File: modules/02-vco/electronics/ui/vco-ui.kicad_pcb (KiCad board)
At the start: 2 copper layers, 58 x 110 mm, 40 parts, among them J1 Conn_01x04, J2 Conn_02x05_Odd_Even, J3 Conn_02x03_Odd_Even, J4 Conn_01x02, J5 Conn_02x02_Counter_Clockwise, J6 Conn_01x07, U1 0203

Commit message: VCO JLCPCB export done for v1.0
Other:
- board text added: "SHMØERGH MODULEUR"
- board text added: "SM-02 VCO UI V1.0 2025 DEC"
- board text removed: "HM-02 VCO UI V0.2 2025 OCT"
- board text removed: "SHMØERGH HOG MODULEUR"

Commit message: KiCAD version updates - PSU + VCO
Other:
- board text added: "SM-02 VCO UI V1.0"
- board text removed: "SM-02 VCO UI V1.0 2025 DEC"
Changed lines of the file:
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@@
 		)
 	)
-	(gr_text "SM-02 VCO UI \nV1.0 2025 DEC"
+	(gr_text "SM-02 VCO UI \nV1.0"
 		(at 153.394 68.5 0)
 		(layer "F.SilkS")
@@
 			(justify left bottom)
 		)
-		(render_cache "SM-02 VCO UI \nV1.0 2025 DEC" 0
+		(render_cache "SM-02 VCO UI \nV1.0" 0
 			(polygon
 				(pts
@@
 				)
 			)
-			(polygon
-				(pts
-					(xy 158.657958 68.011823) (xy 158.657958 68.3045) (xy 159.389789 68.3045) (xy 159.389789 68.158161)
-					(xy 158.804296 68.158161) (xy 158.804296 68.011823)
-				)
-			)
-			(polygon
-				(pts
-					(xy 159.243381 67.279992) (xy 159.243381 67.133584) (xy 158.804296 67.133584) (xy 158.804296 67.279992)
-				)
-			)
-			(polygon
-				(pts
-					(xy 159.243381 67.279992) (xy 159.243381 67.572739) (xy 159.389789 67.572739) (xy 159.389789 67.279992)
-				)
-			)
-			(polygon
-				(pts
-					(xy 158.804296 67.865415) (xy 158.804296 68.011823) (xy 158.950704 68.011823) (xy 158.950704 67.865415)
-				)
-			)
-			(polygon
-				(pts
-					(xy 158.657958 67.279992) (xy 158.657958 67.42633) (xy 158.804296 67.42633) (xy 158.804296 67.279992)
-				)
-			)
-			(polygon
-				(pts
-					(xy 159.097043 67.572739) (xy 159.097043 67.719077) (xy 159.243381 67.719077) (xy 159.243381 67.572739)
-				)
-			)
-			(polygon
-				(pts
-					(xy 158.950704 67.719077) (xy 158.950704 67.865415) (xy 159.097043 67.865415) (xy 159.097043 67.719077)
-				)
-			)
-			(polygon
-				(pts
-					(xy 159.681482 67.279992) (xy 159.681482 68.158161) (xy 159.82782 68.158161) (xy 159.82782 67.865415)
-					(xy 159.974228 67.865415) (xy 159.974228 67.719077) (xy 159.82782 67.719077) (xy 159.82782 67.279992)
-				)
-			)
-			(polygon
-				(pts
-					(xy 159.82782 68.158161) (xy 159.82782 68.3045) (xy 160.266905 68.3045) (xy 160.266905 68.158161)
-				)
-			)
-			(polygon
-				(pts
-					(xy 159.82782 67.133584) (xy 159.82782 67.279992) (xy 160.266905 67.279992) (xy 160.266905 67.133584)
-				)
-			)
-			(polygon
-				(pts
-					(xy 160.266905 67.279992) (xy 160.266905 67.42633) (xy 160.120567 67.42633) (xy 160.120567 67.572739)
-					(xy 160.266905 67.572739) (xy 160.266905 68.158161) (xy 160.413313 68.158161) (xy 160.413313 67.279992)
-				)
-			)
-			(polygon
-				(pts
-					(xy 159.974228 67.572739) (xy 159.974228 67.719077) (xy 160.120567 67.719077) (xy 160.120567 67.572739)
-				)
-			)
-			(polygon
-				(pts
-					(xy 160.705006 68.011823) (xy 160.705006 68.3045) (xy 161.436837 68.3045) (xy 161.436837 68.158161)
-					(xy 160.851344 68.158161) (xy 160.851344 68.011823)
-				)
-			)
-			(polygon
-				(pts
-					(xy 161.290429 67.279992) (xy 161.290429 67.133584) (xy 160.851344 67.133584) (xy 160.851344 67.279992)
-				)
-			)
-			(polygon
-				(pts
-					(xy 161.290429 67.279992) (xy 161.290429 67.572739) (xy 161.436837 67.572739) (xy 161.436837 67.279992)
-				)
-			)
-			(polygon
-				(pts
-					(xy 160.851344 67.865415) (xy 160.851344 68.011823) (xy 160.997753 68.011823) (xy 160.997753 67.865415)
-				)
-			)
-			(polygon
-				(pts
-					(xy 160.705006 67.279992) (xy 160.705006 67.42633) (xy 160.851344 67.42633) (xy 160.851344 67.279992)
-				)
-			)
-			(polygon
-				(pts
-					(xy 161.144091 67.572739) (xy 161.144091 67.719077) (xy 161.290429 67.719077) (xy 161.290429 67.572739)
-				)
-			)
-			(polygon
-				(pts
-					(xy 160.997753 67.719077) (xy 160.997753 67.865415) (xy 161.144091 67.865415) (xy 161.144091 67.719077)
-				)
-			)
-			(polygon
-				(pts
-					(xy 161.72853 67.133584) (xy 161.72853 67.719077) (xy 162.313953 67.719077) (xy 162.313953 67.572739)
-					(xy 161.874868 67.572739) (xy 161.874868 67.279992) (xy 162.460361 67.279992) (xy 162.460361 67.133584)
-				)
-			)
-			(polygon
-				(pts
-					(xy 162.313953 67.719077) (xy 162.313953 68.158161) (xy 162.460361 68.158161) (xy 162.460361 67.719077)
-				)
-			)
-			(polygon
-				(pts
-					(xy 162.313953 68.158161) (xy 161.874868 68.158161) (xy 161.874868 68.3045) (xy 162.313953 68.3045)
-				)
-			)
-			(polygon
-				(pts
-					(xy 161.874868 68.158161) (xy 161.874868 68.011823) (xy 161.72853 68.011823) (xy 161.72853 68.158161)
-				)
-			)
-			(polygon
-				(pts
-					(xy 163.775578 67.133584) (xy 163.775578 68.3045) (xy 164.361001 68.3045) (xy 164.361001 68.158161)
-					(xy 163.921916 68.158161) (xy 163.921916 67.279992) (xy 164.361001 67.279992) (xy 164.361001 67.133584)
-				)
-			)
-			(polygon
-				(pts
-					(xy 164.361001 67.279992) (xy 164.361001 68.158161) (xy 164.507409 68.158161) (xy 164.507409 67.279992)
-				)
-			)
-			(polygon
-				(pts
-					(xy 164.799102 67.133584) (xy 164.799102 68.3045) (xy 165.530933 68.3045) (xy 165.530933 68.158161)
-					(xy 164.945441 68.158161) (xy 164.945441 67.719077) (xy 165.384525 67.719077) (xy 165.384525 67.572739)
-					(xy 164.945441 67.572739) (xy 164.945441 67.279992) (xy 165.530933 67.279992) (xy 165.530933 67.133584)
-				)
-			)
-			(polygon
-				(pts
-					(xy 165.822627 67.279992) (xy 165.822627 68.158161) (xy 165.968965 68.158161) (xy 165.968965 67.279992)
-				)
-			)
-			(polygon
-				(pts
-					(xy 165.968965 68.158161) (xy 165.968965 68.3045) (xy 166.408049 68.3045) (xy 166.408049 68.158161)
-				)
-			)
-			(polygon
-				(pts
-					(xy 166.408049 68.011823) (xy 166.408049 68.158161) (xy 166.554457 68.158161) (xy 166.554457 68.011823)
-				)
-			)
-			(polygon
-				(pts
-					(xy 165.968965 67.133584) (xy 165.968965 67.279992) (xy 166.408049 67.279992) (xy 166.408049 67.133584)
-				)
-			)
-			(polygon
-				(pts
-					(xy 166.408049 67.279992) (xy 166.408049 67.42633) (xy 166.554457 67.42633) (xy 166.554457 67.279992)
-				)
-			)

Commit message: Changed board versioning to 'rev' on VCO and Mixer
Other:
- board text added: "VCO UI REV 1"
- board text removed: "SM-02 VCO UI V1.0"

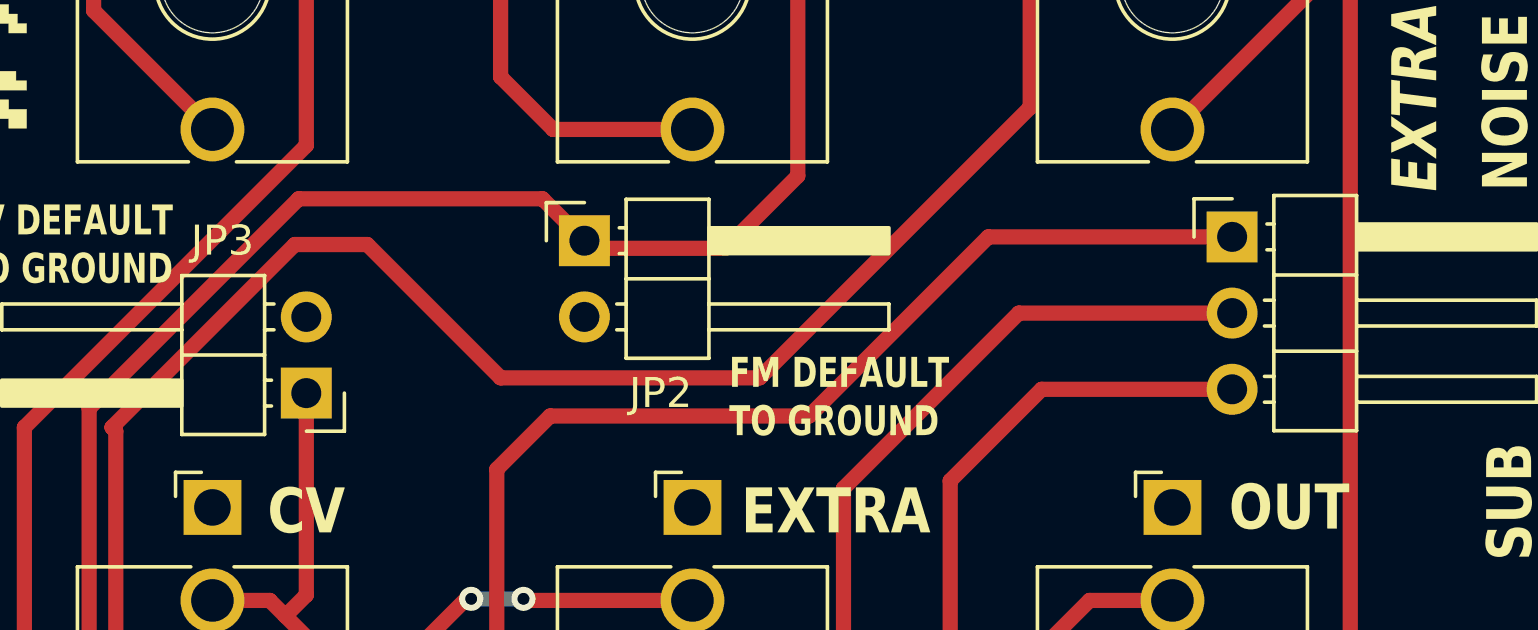
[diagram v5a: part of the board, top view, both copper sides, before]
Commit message: Fixed VCO schemo and PCB after fckckin KiCAD update
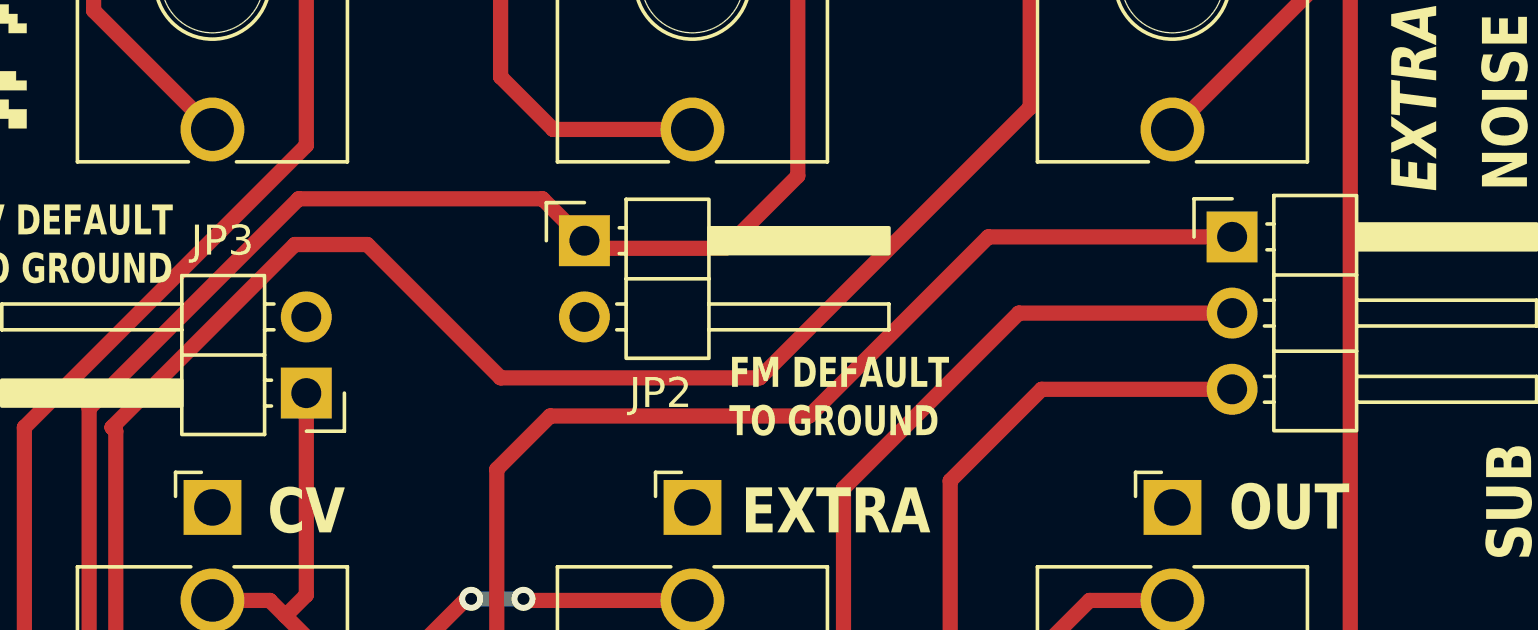
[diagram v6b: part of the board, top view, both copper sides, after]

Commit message: Bumped VCO UI revision no
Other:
- board text added: "VCO UI REV 2"
- board text removed: "VCO UI REV 1"
